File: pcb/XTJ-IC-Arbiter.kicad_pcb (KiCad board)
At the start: 2 copper layers, 80.2 x 66.6 mm, 56 parts, among them IC1 SN74LV125AN, J3 DTM13-12PA-R008, Q1 NPN, U1 LM2675N-5.0/NOPB, U2 CDP68HC68S1, U3 EEC-325X4A, U4 MCP2562-H-P, U5 SP723APP, U6 MCP1700-3302E/TO

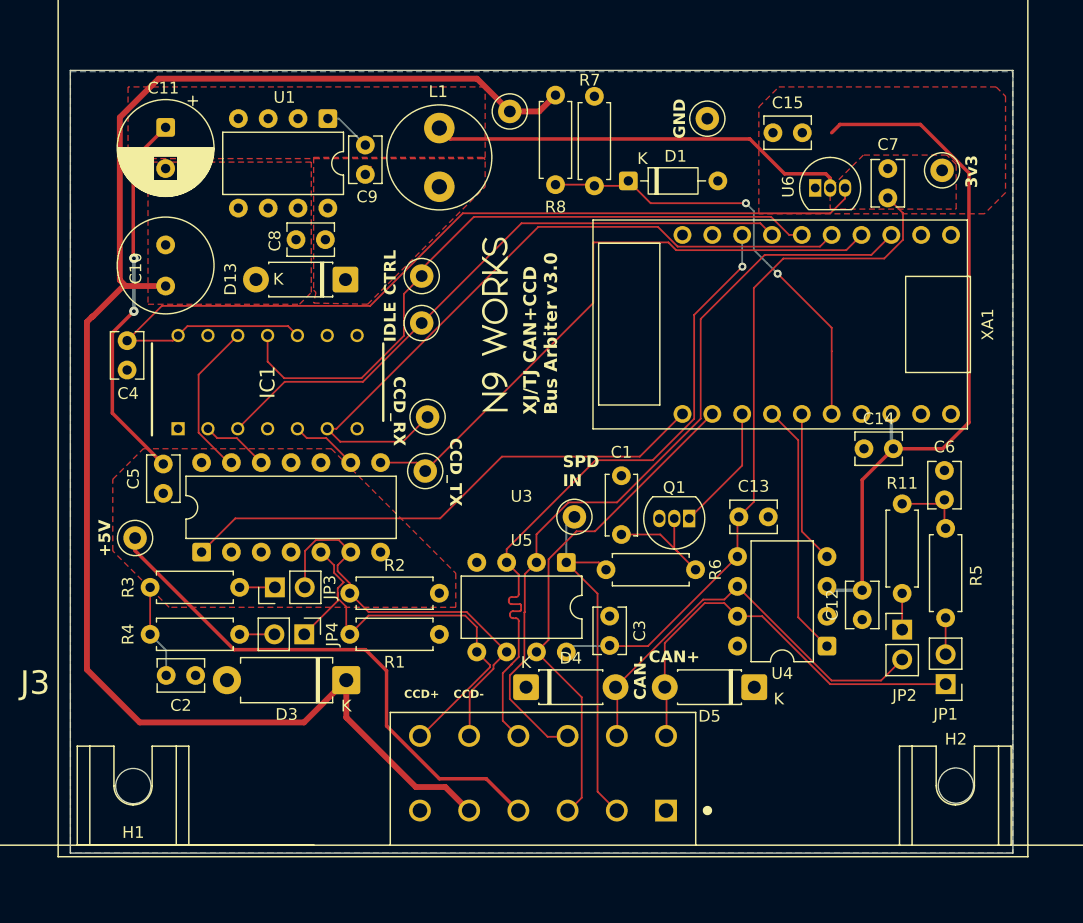
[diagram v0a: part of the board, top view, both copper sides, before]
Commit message: F.Cu ground pour
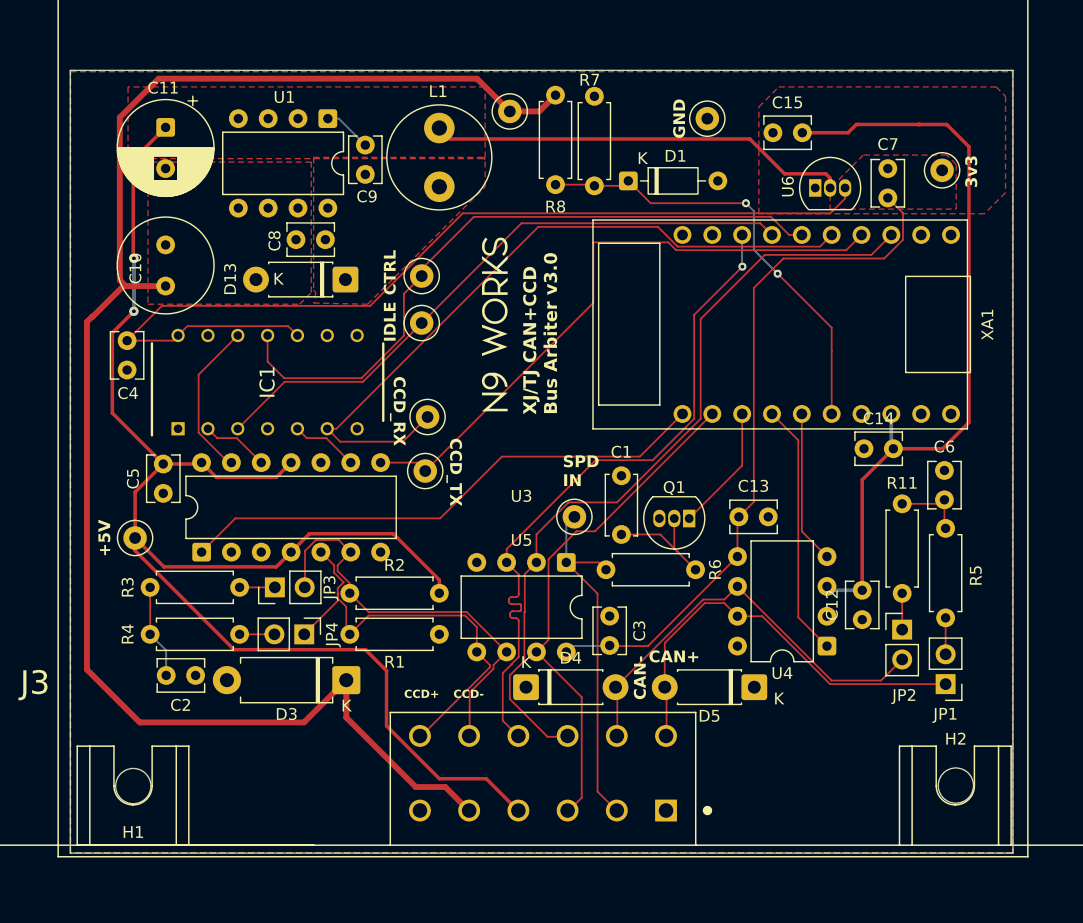
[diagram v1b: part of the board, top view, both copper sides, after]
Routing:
- net +5V: track 174.8 -> 228.9 mm
- added copper zone on F.Cu, net GND
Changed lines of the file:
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@@
+	)
+	(segment
+		(start 108.5558 103.7558)
+		(end 106.1 101.3)
+		(width 0.3)
+		(layer "F.Cu")
+		(net 11)
 	)
 	(segment
@@
 	)
 	(segment
+		(start 167.7 66.0942)
+		(end 167.5 66.0942)
+		(width 0.3)
+		(layer "F.Cu")
+		(net 11)
+	)
+	(segment
 		(start 125.7116 110.8058)
 		(end 114.52983 110.8058)
@@
 	)
 	(segment
-		(start 177.0836 70.224787)
-		(end 172.953013 66.0942)
-		(width 0.3)
-		(layer "F.Cu")
-		(net 11)
-	)
-	(segment
 		(start 114.52983 110.8058)
 		(end 106.1 102.37597)
@@
 	)
 	(segment
+		(start 172.8 66.0942)
+		(end 167.7 66.0942)
+		(width 0.3)
+		(layer "F.Cu")
+		(net 11)
+	)
+	(segment
+		(start 132 104.86863)
+		(end 128.06977 100.9384)
+		(width 0.3)
+		(layer "F.Cu")
+		(net 11)
+	)
+	(segment
+		(start 166.7942 66.8)
+		(end 162.9 66.8)
+		(width 0.3)
+		(layer "F.Cu")
+		(net 11)
+	)
+	(segment
+		(start 113.0158 96.1358)
+		(end 118.1242 96.1358)
+		(width 0.3)
+		(layer "F.Cu")
+		(net 11)
+	)
+	(segment
+		(start 111.76 94.88)
+		(end 113.0158 96.1358)
+		(width 0.3)
+		(layer "F.Cu")
+		(net 11)
+	)
+	(segment
 		(start 105.947349 69.1)
 		(end 108.7 66.347349)
@@
 	)
 	(segment
-		(start 170.65 93.7)
-		(end 174.852362 93.7)
+		(start 128.06977 100.9384)
+		(end 120.9416 100.9384)
+		(width 0.3)
+		(layer "F.Cu")
+		(net 11)
+	)
+	(segment
+		(start 167.5 66.0942)
+		(end 166.7942 66.8)
+		(width 0.3)
+		(layer "F.Cu")
+		(net 11)
+	)
+	(segment
+		(start 119.38 102.5)
+		(end 118.1242 103.7558)
 		(width 0.3)
 		(layer "F.Cu")
@@
 	)
 	(segment
-		(start 166.1058 66.0942)
-		(end 165.4 66.8)
+		(start 174.852362 93.7)
+		(end 170.65 93.7)
+		(width 0.3)
+		(layer "F.Cu")
+		(net 11)
+	)
+	(segment
+		(start 118.1242 96.1358)
+		(end 119.38 94.88)
+		(width 0.3)
+		(layer "F.Cu")
+		(net 11)
+	)
+	(segment
+		(start 108.5 95)
+		(end 111.64 95)
+		(width 0.3)
+		(layer "F.Cu")
+		(net 11)
+	)
+	(segment
+		(start 106.1 101.3)
+		(end 106.1 97.4)
+		(width 0.3)
+		(layer "F.Cu")
+		(net 11)
+	)
+	(segment
+		(start 111.64 95)
+		(end 111.76 94.88)
 		(width 0.3)
 		(layer "F.Cu")
@@
 	)
 	(segment
+		(start 177.0836 91.468762)
+		(end 174.852362 93.7)
+		(width 0.3)
+		(layer "F.Cu")
+		(net 11)
+	)
+	(segment
+		(start 132 106)
+		(end 132 104.86863)
+		(width 0.3)
+		(layer "F.Cu")
+		(net 11)
+	)
+	(segment
+		(start 172.8 66.0942)
+		(end 172.8058 66.1)
+		(width 0.3)
+		(layer "F.Cu")
+		(net 11)
+	)
+	(segment
 		(start 168 105.75)
 		(end 168 96.35)
@@
 	)
 	(segment
-		(start 177.0836 91.468762)
-		(end 177.0836 70.224787)
+		(start 106.1 97.4)
+		(end 108.5 95)
 		(width 0.3)
 		(layer "F.Cu")
@@
 	(segment
 		(start 172.953013 66.0942)
-		(end 166.1058 66.0942)
+		(end 172.8 66.0942)
+		(width 0.3)
+		(layer "F.Cu")
+		(net 11)
+	)
+	(segment
+		(start 175.2 66.1)
+		(end 177.0836 67.9836)
+		(width 0.3)
+		(layer "F.Cu")
+		(net 11)
+	)
+	(segment
+		(start 177.0836 67.9836)
+		(end 177.0836 91.468762)
+		(width 0.3)
+		(layer "F.Cu")
+		(net 11)
+	)
+	(segment
+		(start 120.9416 100.9384)
+		(end 119.38 102.5)
 		(width 0.3)
 		(layer "F.Cu")
@@
 	)
 	(segment
-		(start 174.852362 93.7)
-		(end 177.0836 91.468762)
+		(start 118.1242 103.7558)
+		(end 108.5558 103.7558)
+		(width 0.3)
+		(layer "F.Cu")
+		(net 11)
+	)
+	(segment
+		(start 172.8058 66.1)
+		(end 175.2 66.1)
 		(width 0.3)
 		(layer "F.Cu")
@@
 		(layer "F.Cu")
 		(hatch edge 0.5)
-		(priority 4)
+		(priority 3)
 		(connect_pads
 			(clearance 0)
@@
 		(polygon
 			(pts
-				(xy 109 107.2) (xy 104.2 102.4) (xy 104.2 96.3) (xy 106.8 93.7) (xy 122.8 93.7) (xy 133.4 104.3)
-				(xy 133.4 107.2)
+				(xy 159.2 73.7) (xy 159.2 64.6) (xy 160.9 62.9) (xy 179.4 62.9) (xy 180.2 63.7) (xy 180.2 71.9)
+				(xy 178.4 73.7)
 			)
 		)
 	)
 	(zone
-		(net 11)
-		(net_name "+5V")
+		(net 12)
+		(net_name "GND")
 		(layer "F.Cu")
 		(hatch edge 0.5)
-		(priority 3)
+		(priority 2)
 		(connect_pads
 			(clearance 0)
@@
 		(polygon
 			(pts
-				(xy 159.2 73.7) (xy 159.2 64.6) (xy 160.9 62.9) (xy 179.4 62.9) (xy 180.2 63.7) (xy 180.2 71.9)
-				(xy 178.4 73.7)
+				(xy 100.6 61.5) (xy 180.8 61.5) (xy 180.8 128.1) (xy 100.6 128.1)
 			)
 		)
@@
 		(layer "F.Cu")
 		(hatch edge 0.5)
-		(priority 1)
+		(priority 4)
 		(connect_pads
 			(clearance 0)

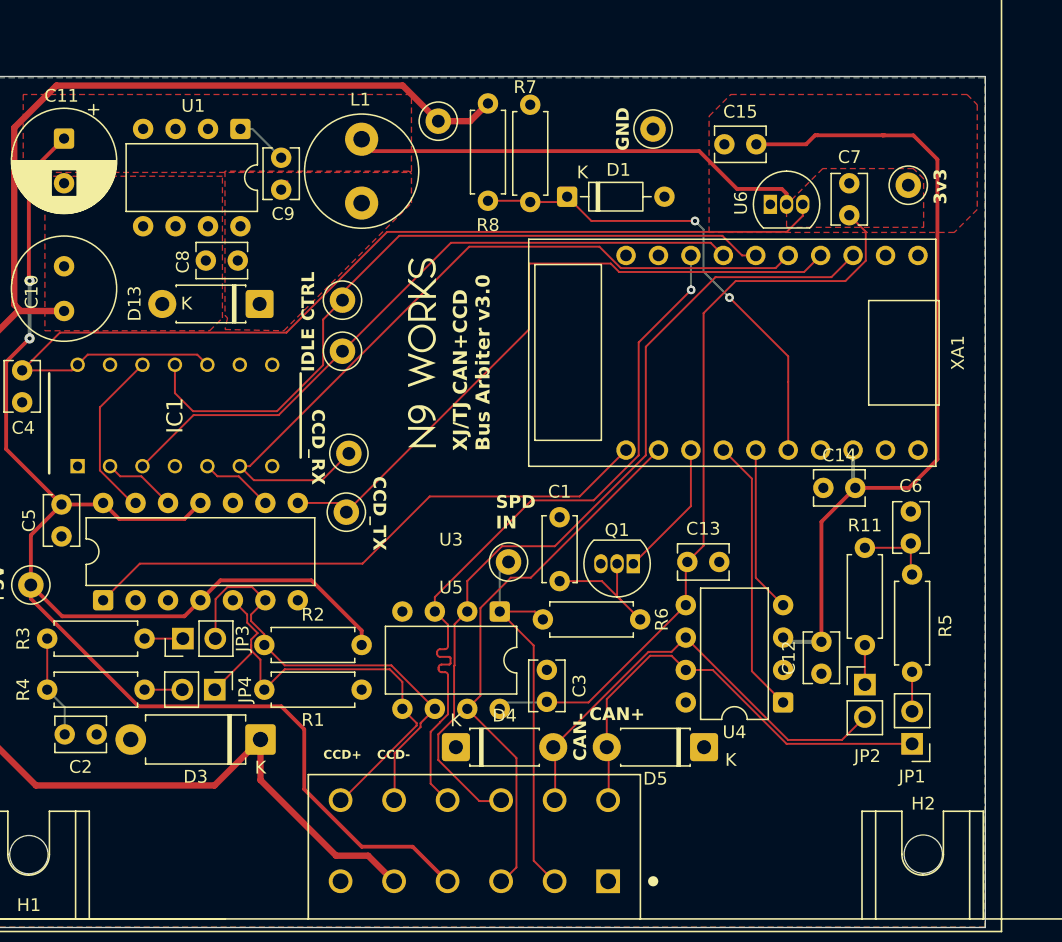
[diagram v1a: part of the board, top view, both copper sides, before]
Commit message: Continued pour zone optimization
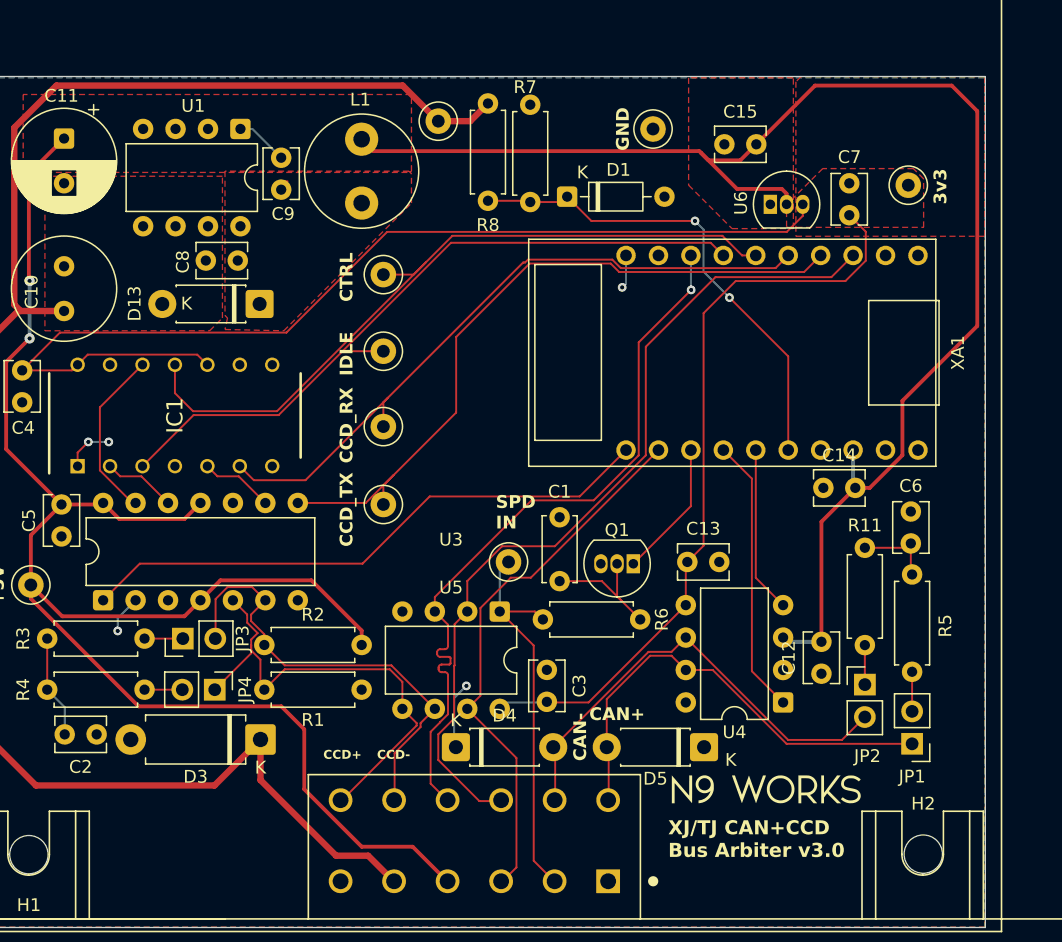
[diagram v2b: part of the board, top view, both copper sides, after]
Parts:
- moved G*** 43.4 mm to (163.6, 117.2), turned to 0 degrees
- moved TP2 3.77 mm to (133.7, 77.0)
- moved TP13 3.42 mm to (133.7, 88.9)
- moved TP3 3.20 mm to (133.7, 83.0)
- moved TP12 2.96 mm to (133.7, 95.0)
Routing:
- net GND: track 0.00 -> 14.5 mm, vias 0 -> 5
- net +5V: track 228.9 -> 241.8 mm
- net ccd_rx: track 61.0 -> 53.6 mm
- net idle: track 53.1 -> 56.3 mm
- net ccd_tx: track 53.1 -> 55.6 mm
- net ctrl: track 56.5 -> 58.3 mm

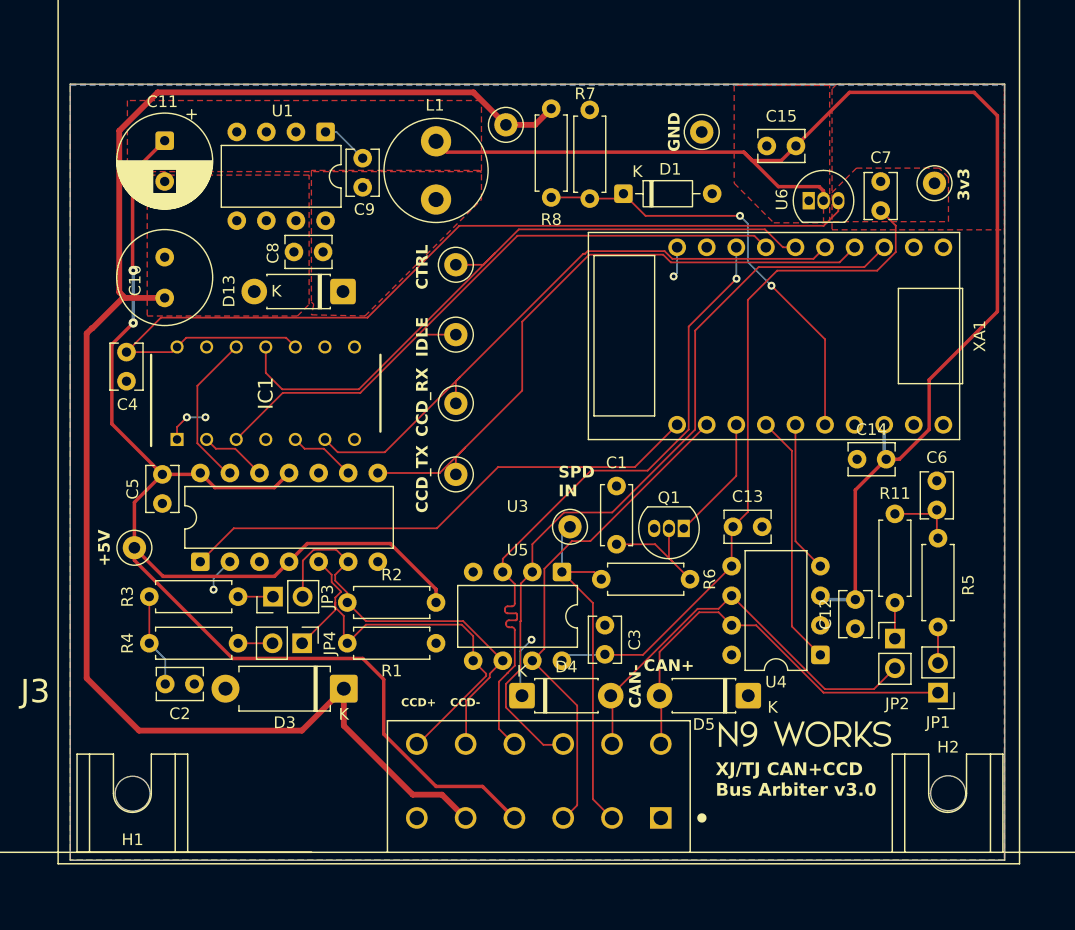
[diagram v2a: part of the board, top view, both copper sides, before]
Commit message: Keep power traces 0.05in from board edge, via rule
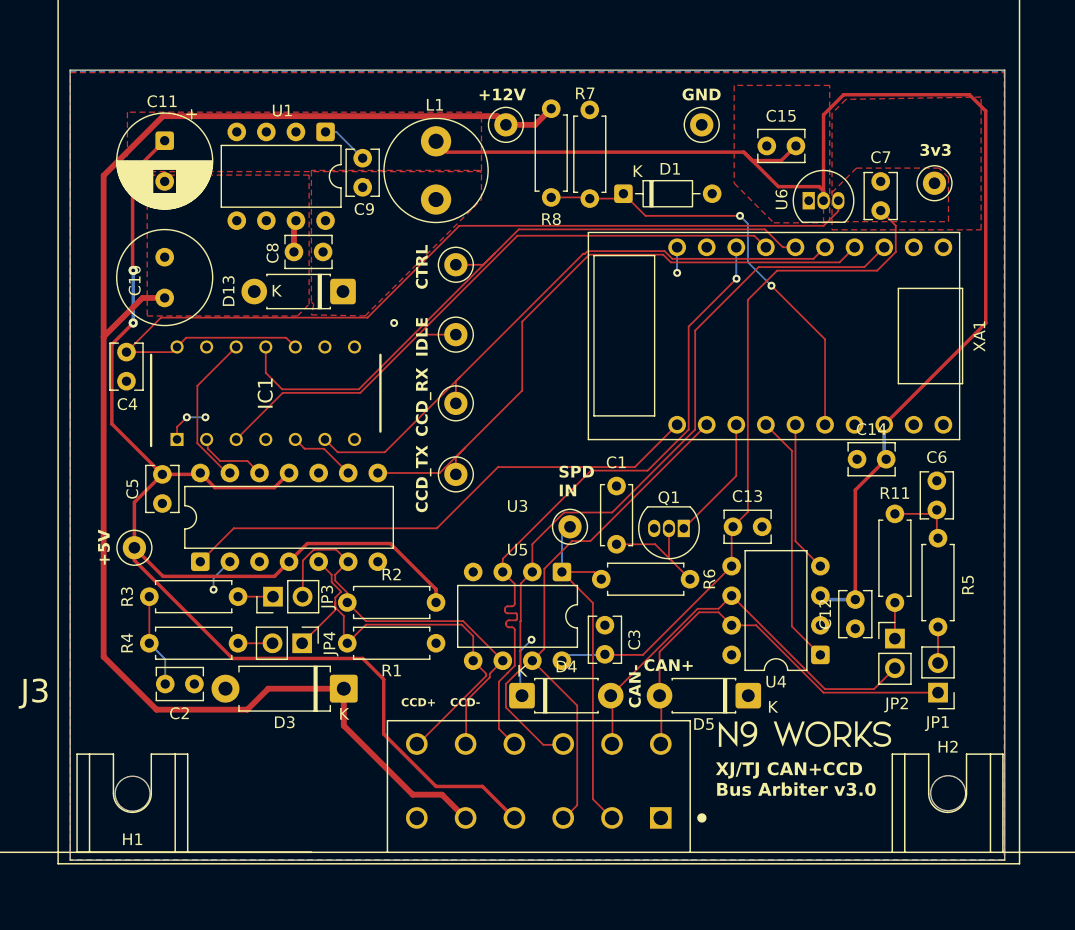
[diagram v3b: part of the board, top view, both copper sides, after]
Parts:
- moved TP5 0.62 mm to (154.8, 65.0)
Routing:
- net +12V: track 135.2 -> 132.4 mm
- net +5V: track 241.8 -> 240.8 mm
- net GND: track 14.5 -> 14.1 mm, vias 5 -> 6
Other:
- board size 80.2 x 66.6 mm -> 80.2 x 67.8 mm
- board text added: "+12V"

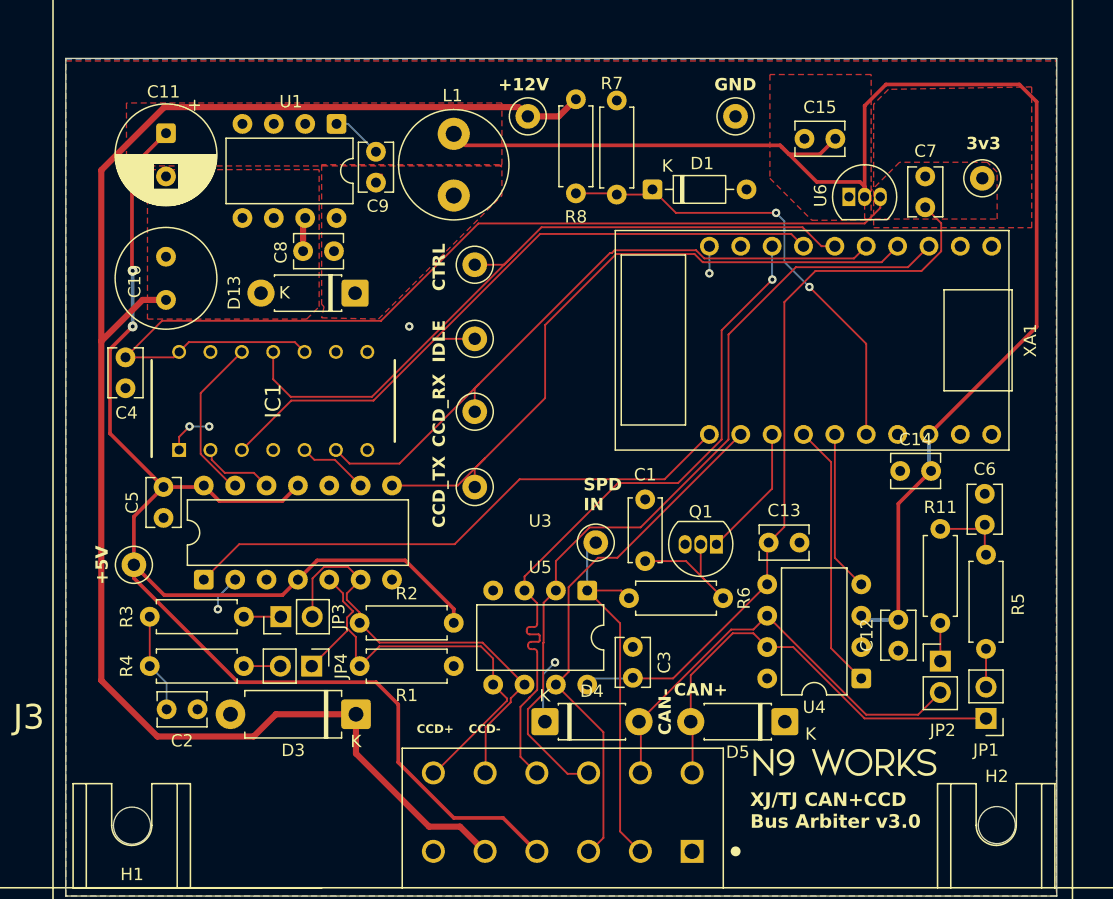
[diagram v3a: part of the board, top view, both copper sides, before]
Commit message: Via stitching
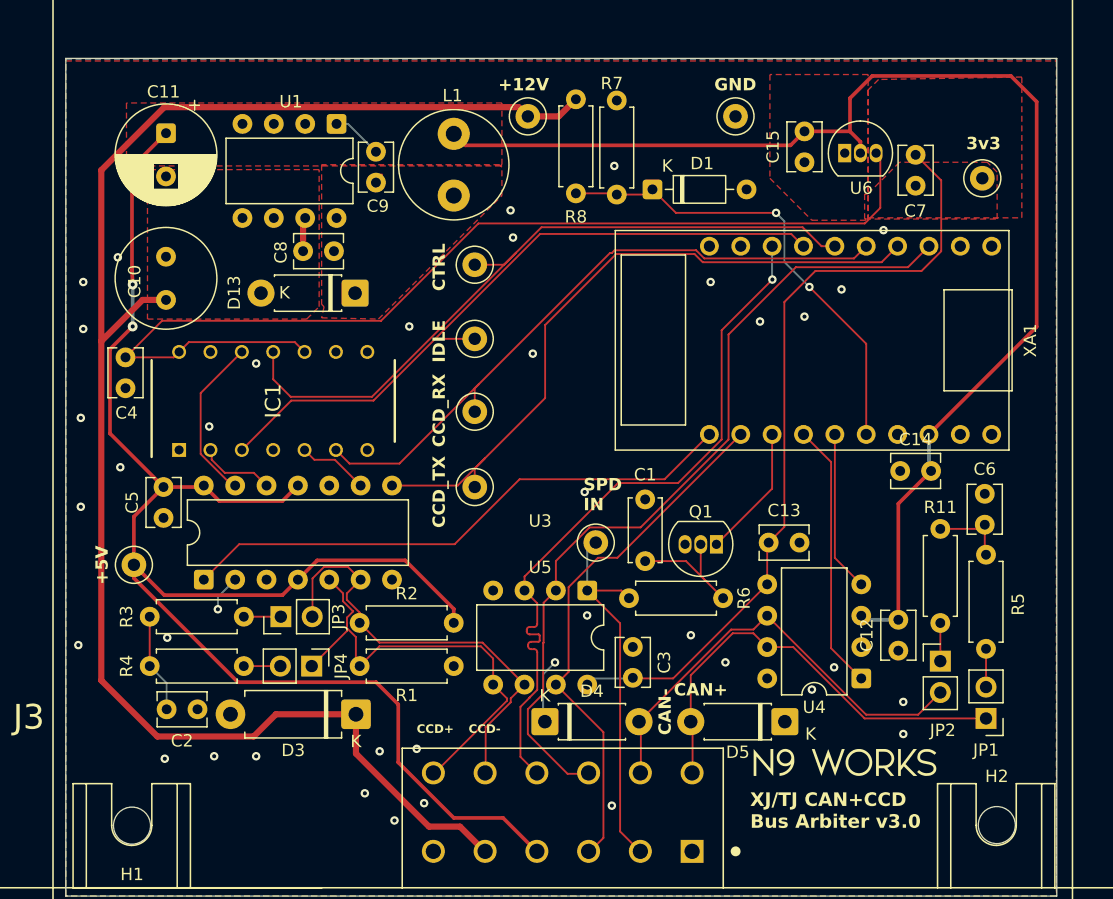
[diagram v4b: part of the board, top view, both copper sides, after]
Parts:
- moved C7 4.32 mm to (169.4, 68.1), turned to -90 degrees
- moved U6 3.56 mm to (163.7, 68.0)
- moved C15 1.90 mm to (160.4, 68.7), turned to 90 degrees
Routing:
- net +5V: track 240.8 -> 231.8 mm
- net +3V3: track 141.4 -> 149.6 mm
- net GND: track 14.1 -> 8.11 mm, vias 6 -> 39
